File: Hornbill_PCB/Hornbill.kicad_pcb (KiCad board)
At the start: 2 copper layers, 90 x 60 mm, 69 parts, among them P1 CONN_01X19, P10 CONN_01X03, P11 CONN_01X03, P12 CONN_01X19, P13 CONN_01X03, P14 CONN_01X09, P15 CONN_01X09, P16 CONN_01X09, P17 CONN_01X09, P18 CONN_01X09, P19 CONN_01X09, P2 CONN_01X19, P20 CONN_01X09, P21 CONN_01X09, P22 CONN_01X09, P23 CONN_01X09, P24 CONN_01X09, P25 CONN_01X13, P26 CONN_01X13, P27 CONN_01X13, P28 CONN_01X13, P29 CONN_01X09, P3 CONN_01X19, P30 CONN_01X09, P4 CONN_01X19, P5 CONN_01X19, P6 CONN_01X19, P7 CONN_01X03, P8 CONN_01X19, P9 CONN_01X03, Q1 Q_NPN_BCE, U1 SHT31_DIS, U2 SD_Crard, U3 RGB_4pin, U4 ESP32_Breakout1, U5 MountingHole, U6 MountingHole, U7 MountingHole, U8 MountingHole

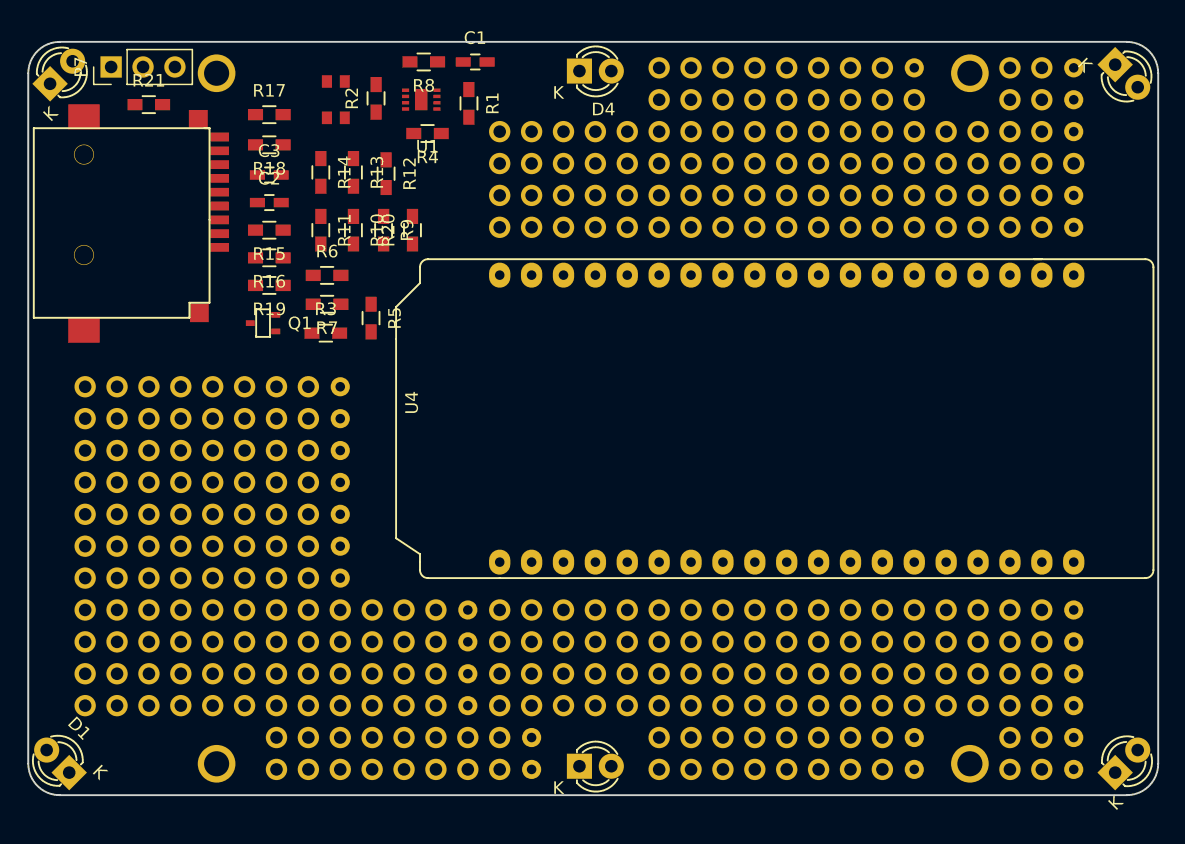
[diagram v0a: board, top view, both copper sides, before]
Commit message: PCB layout routing completed
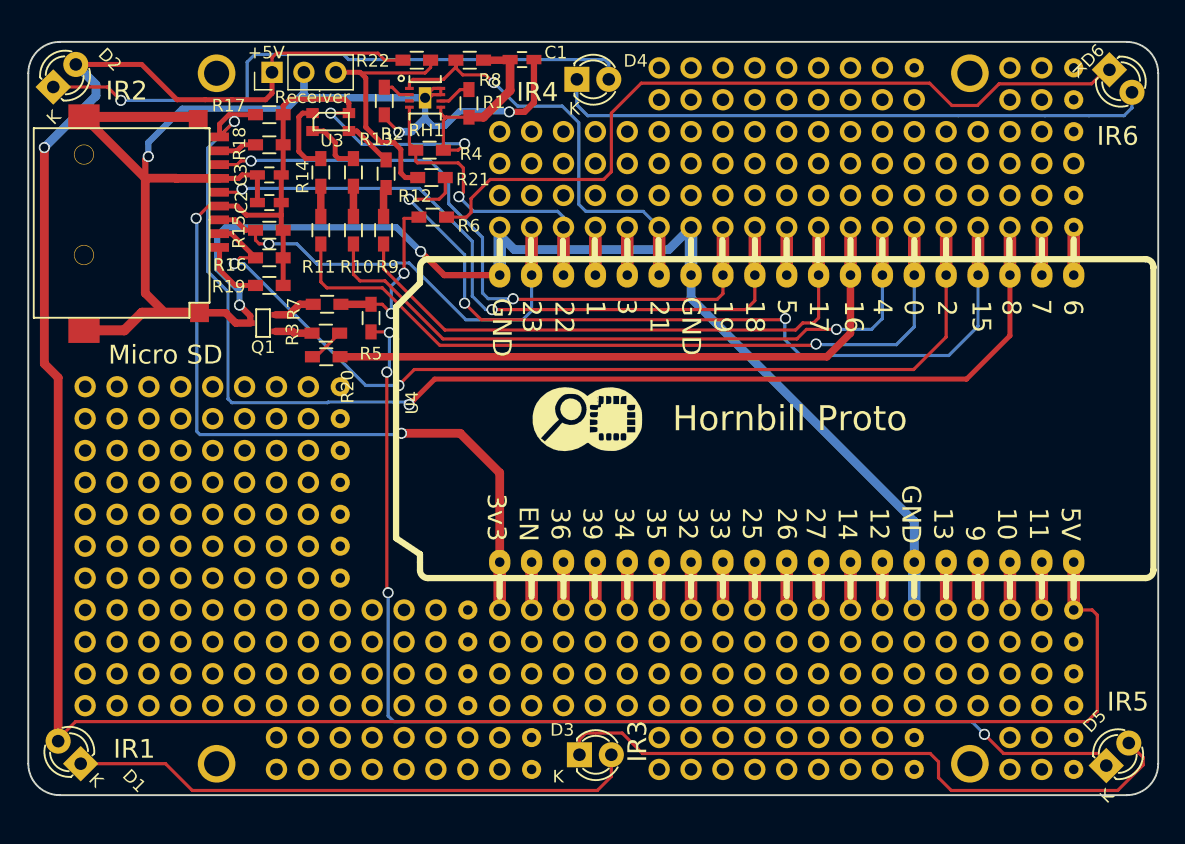
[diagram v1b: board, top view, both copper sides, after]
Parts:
- removed U1: SHT31_DIS, ee:SHT31_DIS
- added P14: CONN_01X01, EElib:Logo_8, F.Cu at (89.4, 80.0)
- added P14: CONN_01X01, EElib:Logo_8, B.Cu at (118.9, 80.3)
- added R22: 0r, Resistors_SMD:R_0603_HandSoldering, F.Cu at (75.9, 51.5)
- added RH1: SHT31-DIS, nosuz lib:DFN-8_SHT-3x-DIS, F.Cu at (76.6, 54.5)
- C1: value 100nF -> 10uF
- moved R21 23.3 mm to (77.1, 60.8), turned to 180 degrees
- moved P7 12.8 mm to (64.4, 52.4)
- moved R20 12.2 mm to (68.7, 75.1), turned to 0 degrees
- moved R6 9.61 mm to (77.2, 64.0)
- moved C1 3.73 mm to (84.3, 51.4)
- moved R8 3.67 mm to (80.2, 51.5)
- moved U3 1.83 mm to (69.1, 56.4), turned to 180 degrees
- moved R4 1.33 mm to (77.0, 58.6)
- moved D1 1.16 mm to (49.2, 107.5)
- moved D3 0.91 mm to (88.9, 106.8)
- moved D5 0.90 mm to (130.9, 107.6)
- moved D4 0.69 mm to (88.7, 53.0)
- moved R2 0.69 mm to (73.4, 54.7), turned to 270 degrees
- moved D6 0.61 mm to (131.1, 52.2)
- moved D2 0.36 mm to (47.0, 53.6)
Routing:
- net GND: track 0.00 -> 199.9 mm, vias 0 -> 5
- net +5V: track 0.00 -> 184.8 mm, vias 0 -> 1
- net 3.3V: track 0.00 -> 111.2 mm, vias 0 -> 4
- net /SD_DTCT: track 0.00 -> 103.0 mm, vias 0 -> 2
- net Net-(D5-Pad1): track 0.00 -> 91.2 mm, vias 0 -> 4
- net /SSEL: track 0.00 -> 76.6 mm, vias 0 -> 2
- net /IR_Rx: track 0.00 -> 67.0 mm, vias 0 -> 3
- net Net-(D6-Pad1): track 0.00 -> 62.5 mm
- net /R: track 0.00 -> 61.0 mm, vias 0 -> 1
- net /CLK: track 0.00 -> 55.5 mm, vias 0 -> 2
- net /G: track 0.00 -> 54.6 mm, vias 0 -> 1
- net /MISO: track 0.00 -> 54.0 mm, vias 0 -> 2
- net Net-(D3-Pad1): track 0.00 -> 52.0 mm
- net /IR_Tx: track 0.00 -> 49.9 mm
- net Net-(D2-Pad1): track 0.00 -> 49.4 mm, vias 0 -> 1
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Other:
- net class Default: clearance 0.254 -> 0.15; trace_width 0.254 -> 0.25; via_dia 0.889 -> 0.6; via_drill 0.635 -> 0.4
- rule trace_clearance: 0.254 -> 0.15
- rule trace_min: 0.254 -> 0.15
- rule via_min_drill: 0.508 -> 0.2
- rule via_min_size: 0.889 -> 0.5
- board text added: "+5V"
- board text added: "0"
- board text added: "1"
- board text added: "10"
- board text added: "11"
- board text added: "12"
- board text added: "13"
- board text added: "14"
- board text added: "15"
- board text added: "16"
- board text added: "17"
- board text added: "18"
- board text added: "19"
- board text added: "2"
- board text added: "21"
- board text added: "22"
- board text added: "23"
- board text added: "25"
- board text added: "26"
- board text added: "27"
- board text added: "3"
- board text added: "32"
- board text added: "33"
- board text added: "34"
- board text added: "35"
- board text added: "36"
- board text added: "39"
- board text added: "3v3"
- board text added: "4"
- board text added: "5"
- board text added: "5V"
- board text added: "6"
- board text added: "7"
- board text added: "8"
- board text added: "9"
- board text added: "EN"
- board text added: "ExploreEmbedded.com"
- board text added: "GND"
- board text added: "Hornbill Proto"
- board text added: "IR1"
- board text added: "IR2"
- board text added: "IR3"
- board text added: "IR4"
- board text added: "IR5"
- board text added: "IR6"
- board text added: "Micro SD"
- board text added: "Receiver"
- board text added: "v0.1"

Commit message: Chnges done as per issues
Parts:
- removed D3, D4: LED, LEDs:LED-3MM
- removed R15: 10k, Resistors_SMD:R_0603_HandSoldering
- removed R16: 10K, Resistors_SMD:R_0603_HandSoldering
- removed R17: 1K, Resistors_SMD:R_0603_HandSoldering
- removed R18, R19: 33K, Resistors_SMD:R_0603_HandSoldering
- added P31: CONN_01X03, Pin_Headers:Pin_Header_Straight_1x03_Pitch2.54mm, F.Cu at (87.6, 108.0)
- added P32: CONN_01X03, Pin_Headers:Pin_Header_Straight_1x03_Pitch2.54mm, F.Cu at (87.6, 52.1)
- added P33: CONN_01X03, Pin_Headers:Pin_Header_Straight_1x03_Pitch2.54mm, F.Cu at (87.6, 54.6)
- added P34: CONN_01X03, Pin_Headers:Pin_Header_Straight_1x03_Pitch2.54mm, F.Cu at (87.6, 105.4)
- Q1: value Q_NPN_BCE -> Q_NPN_BEC; footprint ee:SOT_23 -> EE:SOT_23
- moved C3 0.48 mm to (64.5, 61.0), turned to 180 degrees
- moved C2 0.45 mm to (64.5, 63.1), turned to 180 degrees
- moved Q1 0.25 mm to (63.8, 72.6), turned to 0 degrees
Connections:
- net /CLK renamed /IO18
- net /MISO renamed /IO19
- D5 pad 2: Net-(D3-Pad1) -> Net-(D1-Pad1)
- D6 pad 2: Net-(D4-Pad1) -> Net-(D2-Pad1)
- P3 pad 10: Net-(P3-Pad10) -> /IO5
- P3 pad 18: /MOSI -> /IO23
- P3 pad 3: /SD_DTCT -> Net-(P3-Pad3)
- P3 pad 5: /SSEL -> Net-(P3-Pad5)
- P3 pad 6: /R -> Net-(P3-Pad6)
- P3 pad 7: /G -> Net-(P3-Pad7)
- P3 pad 9: /B -> Net-(P3-Pad9)
- P4 pad 10: Net-(P4-Pad10) -> /G
- P4 pad 11: Net-(P4-Pad11) -> /R
- P4 pad 9: Net-(P4-Pad9) -> /B
- Q1 pad 2: Net-(Q1-Pad2) -> GND
- Q1 pad 3: GND -> Net-(Q1-Pad3)
- R7 pad 2: Net-(Q1-Pad2) -> Net-(Q1-Pad3)
- U2 pad 1: Net-(R19-Pad2) -> /IO5
- U2 pad 2: /SSEL -> /IO23
- U2 pad 3: /MOSI -> GND
- U2 pad 9: /SD_DTCT -> Net-(U2-Pad9)
- U4 pad 10: Net-(P3-Pad10) -> /IO5
- U4 pad 18: /MOSI -> /IO23
- U4 pad 28: Net-(P4-Pad11) -> /R
- U4 pad 29: Net-(P4-Pad10) -> /G
- U4 pad 3: /SD_DTCT -> Net-(P3-Pad3)
- U4 pad 30: Net-(P4-Pad9) -> /B
- U4 pad 5: /SSEL -> Net-(P3-Pad5)
- U4 pad 6: /R -> Net-(P3-Pad6)
- U4 pad 7: /G -> Net-(P3-Pad7)
- U4 pad 9: /B -> Net-(P3-Pad9)
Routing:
- net /SD_DTCT: track 103.0 -> 0.00 mm, vias 2 -> 0
- net /SSEL: track 76.6 -> 0.00 mm, vias 2 -> 0
- net /IO5: track 0.00 -> 54.6 mm
- net Net-(D3-Pad1): track 52.0 -> 0.00 mm
- net Net-(D4-Pad1): track 48.1 -> 0.00 mm
- net Net-(D1-Pad1): track 45.3 -> 92.6 mm
- net Net-(D2-Pad1): track 49.4 -> 94.5 mm
- net /IO23: track 0.00 -> 42.1 mm, vias 0 -> 1
- net /MOSI: track 35.6 -> 0.00 mm, vias 1 -> 0
- net /B: track 46.3 -> 54.8 mm, vias 0 -> 1
- net Net-(R5-Pad1): track 13.7 -> 21.9 mm
- net GND: track 199.9 -> 193.3 mm, vias 5 -> 3
- net Net-(R19-Pad2): track 5.16 -> 0.00 mm
- net /R: track 61.0 -> 56.2 mm
- net Net-(Q1-Pad3): track 0.00 -> 4.55 mm
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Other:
- board text added: "v0.2"
- board text removed: "IR5"
- board text removed: "IR6"
- board text removed: "v0.1"

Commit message: Logo and Gerber files generted for v0.2
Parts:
- removed the P14 at (118.9, 80.3)
- added G***: LOGO, Hornbill proto logo:Hornbill_ESP32_Proto, B.Cu at (102.6, 80.9)
- moved P14 1.60 mm to (90.9, 79.4)
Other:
- board text removed: "Hornbill Proto"
